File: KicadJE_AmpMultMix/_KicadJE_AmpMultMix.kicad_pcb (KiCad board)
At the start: 2 copper layers, 100 x 100 mm, 28 parts, among them J201 In1.1, J202 In1.2, J203 In1.3, J204 Out1, J205 In2, J206 Out2.1, J207 Out2.2, J208 Out2.3, P201 HEADER_2x5_Doepfer, SW201 Inv/NonInv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

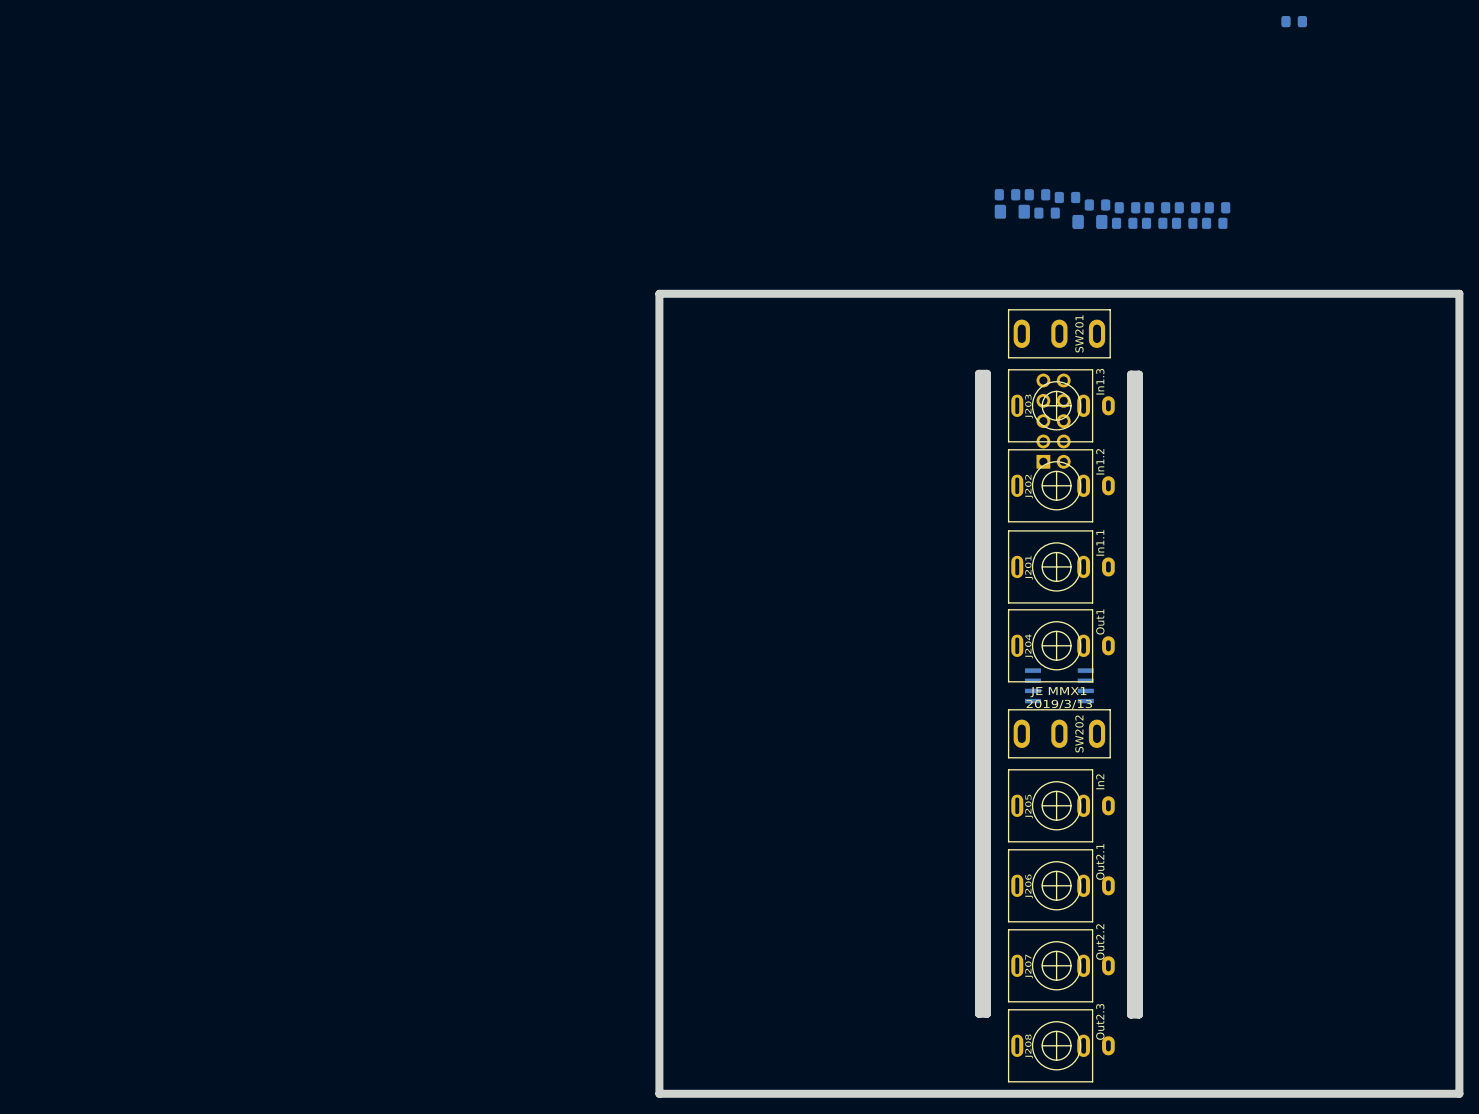
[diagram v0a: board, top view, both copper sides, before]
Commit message: JE MMX1 - Front components placed
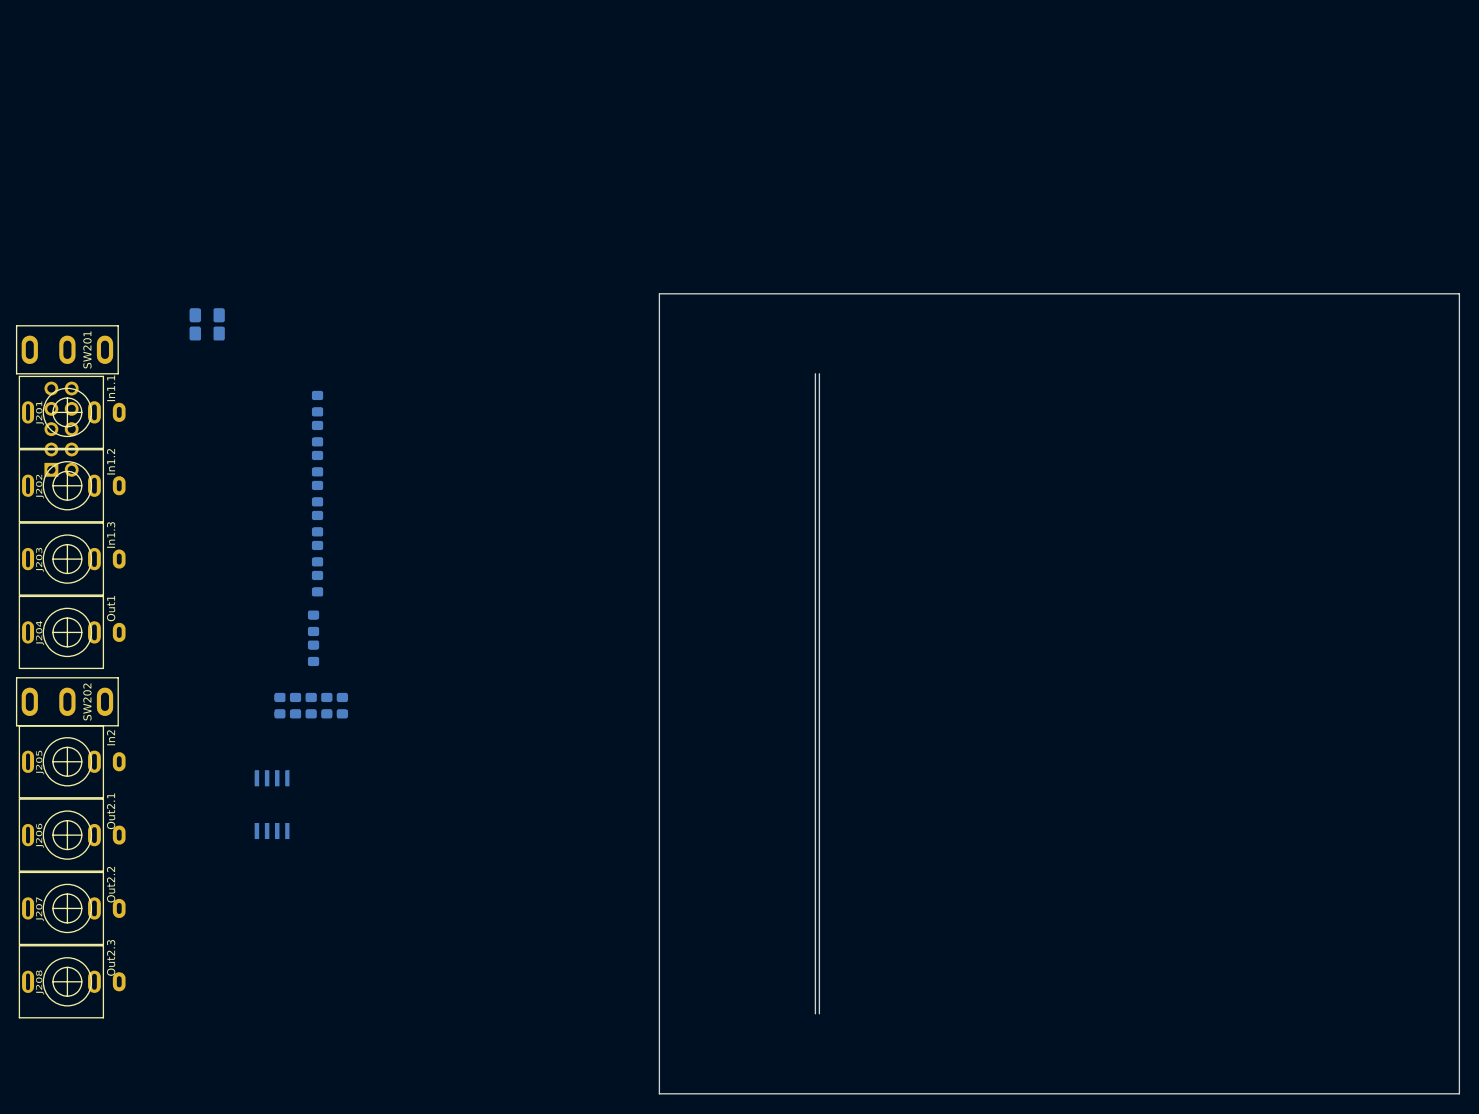
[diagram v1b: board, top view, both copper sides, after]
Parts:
- moved R210 151.3 mm to (54.5, 101.5), turned to 270 degrees
- moved R213 128.0 mm to (56.5, 101.5), turned to 270 degrees
- moved J201 125.1 mm to (26.0, 64.8)
- moved J203 125.1 mm to (26.0, 83.2)
- moved R214 124.3 mm to (58.4, 101.5), turned to 270 degrees
- moved SW202 124.1 mm to (26.0, 101.0)
- moved SW201 124.0 mm to (26.0, 57.0)
- moved P201 124.0 mm to (24.0, 72.0)
- moved J208 123.9 mm to (26.0, 136.0)
- moved J207 123.9 mm to (26.0, 126.8)
- moved J206 123.8 mm to (26.0, 117.7)
- moved J205 123.8 mm to (26.0, 108.5)
- moved J204 123.7 mm to (26.0, 92.3)
- moved J202 123.7 mm to (26.0, 74.0)
- moved R212 121.4 mm to (56.8, 94.9), turned to 270 degrees
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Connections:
- J204 pad TN: Net-(J204-PadTN) -> (no net)
- J206 pad TN: Net-(J206-PadTN) -> (no net)
- J207 pad TN: Net-(J207-PadTN) -> (no net)
- J208 pad TN: Net-(J208-PadTN) -> (no net)
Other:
- outline, holes or cut-outs redrawn
- net class Power removed
- rule pad_to_mask_clearance: 0.2 -> 0.051
- board text removed: "JE MMX1 2019/3/13"
